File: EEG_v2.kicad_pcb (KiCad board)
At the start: 2 copper layers, 114 parts, among them P1 CONN_2, P2 CONN_8, P3 USB_A, P4 CONN_8, P5 CONN_5X2, P6 CONN_2, P7 CONN_1, SW1 SWITCH_INV, SW2 RESET, SW3 SW_PUSH_4PIN, SW4 SW_PUSH_4PIN, U1 ADS1299IPAGR, U2 TLV70033, U3 TLV70025, U4 LM2664, U5 TPS72325, U6 CC2540, U7 2450BM15A0002E, X1 QUARTZCMS4_32K, X2 32-MHz

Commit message: Continue layout.
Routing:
- net N-0000096: track 0.00 -> 1.18 mm
- net N-0000094: track 0.00 -> 1.18 mm
- net N-0000093: track 0.00 -> 1.18 mm
- net N-0000092: track 0.00 -> 1.18 mm
- net N-0000091: track 0.00 -> 1.18 mm
- net N-0000090: track 0.00 -> 1.18 mm
- net N-0000089: track 0.00 -> 1.18 mm
- net N-0000088: track 0.00 -> 1.18 mm
- net N-0000078: track 0.00 -> 1.18 mm
- net N-0000077: track 0.00 -> 1.18 mm
- net N-0000076: track 0.00 -> 1.18 mm
- net N-0000070: track 0.00 -> 1.18 mm
- net N-0000067: track 0.00 -> 1.18 mm
- net N-0000095: track 0.00 -> 1.18 mm
- net N-0000079: track 0.00 -> 1.18 mm
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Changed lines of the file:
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@@
   (general
     (links 295)
-    (no_connects 193)
+    (no_connects 177)
     (area 249.516999 132.753099 336.86877 191.129001)
     (thickness 1.6)
-    (drawings 0)
-    (tracks 263)
+    (drawings 1)
+    (tracks 295)
     (zones 0)
     (modules 114)
@@
     )
   )
+  (dimension 43.501839 (width 0.3) (layer F.SilkS)
+    (gr_text "43.502 mm" (at 345.328961 154.844059 89.47315711) (layer F.SilkS)
+      (effects (font (size 1.5 1.5) (thickness 0.3)))
+    )
+    (feature1 (pts (xy 334.9 176.5) (xy 346.478904 176.606472)))
+    (feature2 (pts (xy 335.3 133) (xy 346.878904 133.106472)))
+    (crossbar (pts (xy 344.179019 133.081646) (xy 343.779019 176.581646)))
+    (arrow1a (pts (xy 343.779019 176.581646) (xy 343.202982 175.449798)))
+    (arrow1b (pts (xy 343.779019 176.581646) (xy 344.375773 175.460583)))
+    (arrow2a (pts (xy 344.179019 133.081646) (xy 343.582265 134.202709)))
+    (arrow2b (pts (xy 344.179019 133.081646) (xy 344.755056 134.213494)))
+  )
   (segment (start 311.85184 165.74816) (end 311.85184 165.35184) (width 0.254) (layer F.Cu) (net 1))
   (segment (start 310.93156 164.43156) (end 310.93156 162.90544) (width 0.254) (layer F.Cu) (net 1))
@@
   (segment (start 305.27116 172.67884) (end 305.27116 170.58) (width 0.254) (layer F.Cu) (net 59))
   (segment (start 304.957 172.993) (end 305.27116 172.67884) (width 0.254) (layer F.Cu) (net 59))
+  (segment (start 327.1005 142.9385) (end 327.1005 143.9815) (width 0.254) (layer F.Cu) (net 66) (status C00000))
+  (segment (start 327.1005 143.9815) (end 327.2005 144.0815) (width 0.254) (layer F.Cu) (net 66) (status C00000))
+  (segment (start 327.1005 137.3505) (end 327.1005 136.3075) (width 0.254) (layer F.Cu) (net 67) (status C00000))
+  (segment (start 327.1005 136.3075) (end 327.2005 136.2075) (width 0.254) (layer F.Cu) (net 67) (status C00000))
+  (segment (start 327.1005 138.4935) (end 327.1005 139.5365) (width 0.254) (layer F.Cu) (net 68) (status C00000))
+  (segment (start 327.1005 139.5365) (end 327.2005 139.6365) (width 0.254) (layer F.Cu) (net 68) (status C00000))
+  (segment (start 327.1005 147.3835) (end 327.1005 148.4265) (width 0.254) (layer F.Cu) (net 69) (status C00000))
+  (segment (start 327.1005 148.4265) (end 327.2005 148.5265) (width 0.254) (layer F.Cu) (net 69) (status C00000))
+  (segment (start 327.1005 141.7955) (end 327.1005 140.7525) (width 0.254) (layer F.Cu) (net 70) (status C00000))
+  (segment (start 327.1005 140.7525) (end 327.2005 140.6525) (width 0.254) (layer F.Cu) (net 70) (status C00000))
+  (segment (start 327.1005 146.2405) (end 327.1005 145.1975) (width 0.254) (layer F.Cu) (net 71) (status C00000))
+  (segment (start 327.1005 145.1975) (end 327.2005 145.0975) (width 0.254) (layer F.Cu) (net 71) (status C00000))
+  (segment (start 327.1005 150.6855) (end 327.1005 149.6425) (width 0.254) (layer F.Cu) (net 72) (status C00000))
+  (segment (start 327.1005 149.6425) (end 327.2005 149.5425) (width 0.254) (layer F.Cu) (net 72) (status C00000))
+  (segment (start 327.1005 169.7355) (end 327.1005 170.7785) (width 0.254) (layer F.Cu) (net 74) (status C00000))
+  (segment (start 327.1005 170.7785) (end 327.2005 170.8785) (width 0.254) (layer F.Cu) (net 74) (status C00000))
+  (segment (start 327.1005 168.5925) (end 327.1005 167.5495) (width 0.254) (layer F.Cu) (net 75) (status C00000))
+  (segment (start 327.1005 167.5495) (end 327.2005 167.4495) (width 0.254) (layer F.Cu) (net 75) (status C00000))
+  (segment (start 327.1005 159.5755) (end 327.1005 158.5325) (width 0.254) (layer F.Cu) (net 76) (status C00000))
+  (segment (start 327.1005 158.5325) (end 327.2005 158.4325) (width 0.254) (layer F.Cu) (net 76) (status C00000))
+  (segment (start 327.1005 160.7185) (end 327.1005 161.7615) (width 0.254) (layer F.Cu) (net 77) (status C00000))
+  (segment (start 327.1005 161.7615) (end 327.2005 161.8615) (width 0.254) (layer F.Cu) (net 77) (status C00000))
+  (segment (start 327.1005 164.0205) (end 327.1005 162.9775) (width 0.254) (layer F.Cu) (net 78) (status C00000))
+  (segment (start 327.1005 162.9775) (end 327.2005 162.8775) (width 0.254) (layer F.Cu) (net 78) (status C00000))
+  (segment (start 327.1005 165.1635) (end 327.1005 166.2065) (width 0.254) (layer F.Cu) (net 79) (status C00000))
+  (segment (start 327.1005 166.2065) (end 327.2005 166.3065) (width 0.254) (layer F.Cu) (net 79) (status C00000))
+  (segment (start 327.1005 151.8285) (end 327.1005 152.8715) (width 0.254) (layer F.Cu) (net 80) (status C00000))
+  (segment (start 327.1005 152.8715) (end 327.2005 152.9715) (width 0.254) (layer F.Cu) (net 80) (status C00000))
+  (segment (start 327.1005 156.2735) (end 327.1005 157.3165) (width 0.254) (layer F.Cu) (net 81) (status C00000))
+  (segment (start 327.1005 157.3165) (end 327.2005 157.4165) (width 0.254) (layer F.Cu) (net 81) (status C00000))
+  (segment (start 327.1005 155.1305) (end 327.1005 154.0875) (width 0.254) (layer F.Cu) (net 82) (status C00000))
+  (segment (start 327.1005 154.0875) (end 327.2005 153.9875) (width 0.254) (layer F.Cu) (net 82) (status C00000))
   (segment (start 292.9415 144.5455) (end 291.252 144.5455) (width 0.254) (layer F.Cu) (net 83))
   (segment (start 291.252 144.5455) (end 290.75 145.0475) (width 0.254) (layer F.Cu) (net 83))

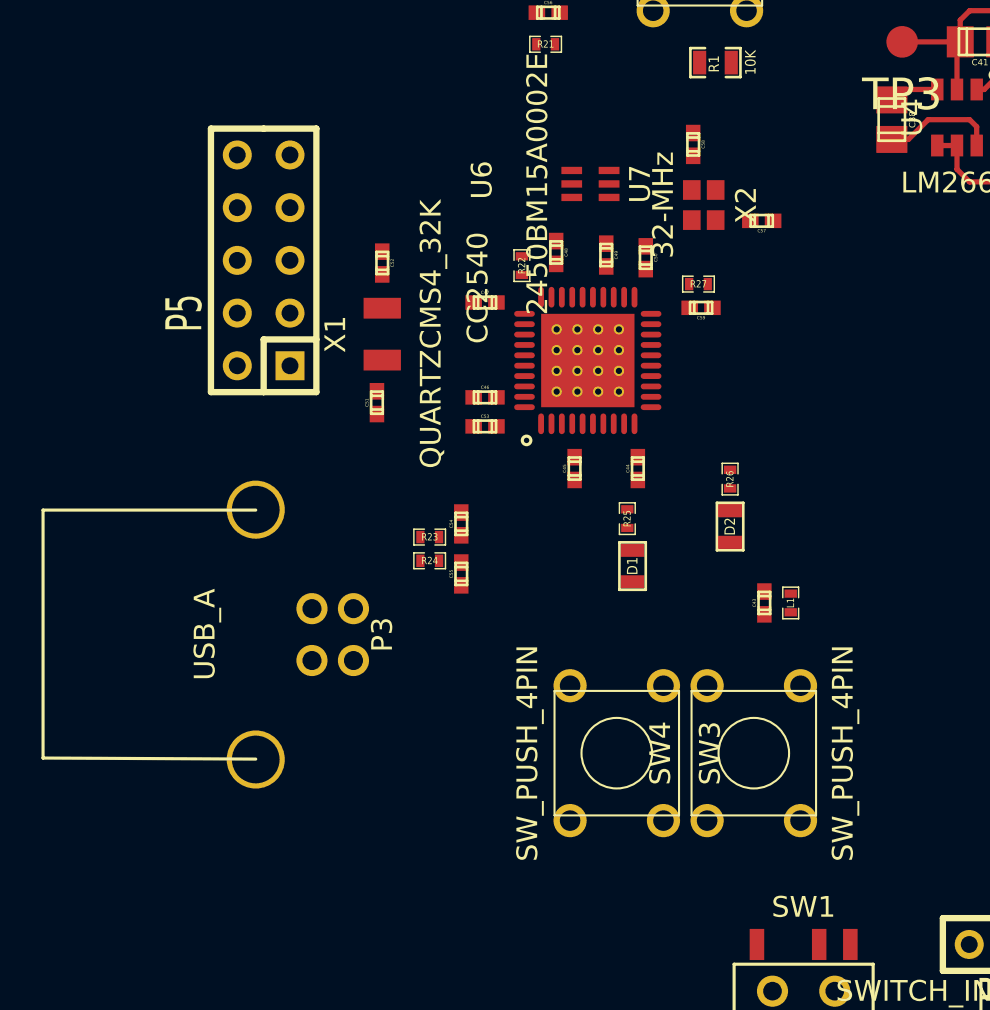
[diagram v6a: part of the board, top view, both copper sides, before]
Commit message: Continue layout for CC2540
Change swiches to one pin operating to clear under space. Edit USB conn
to show back size.
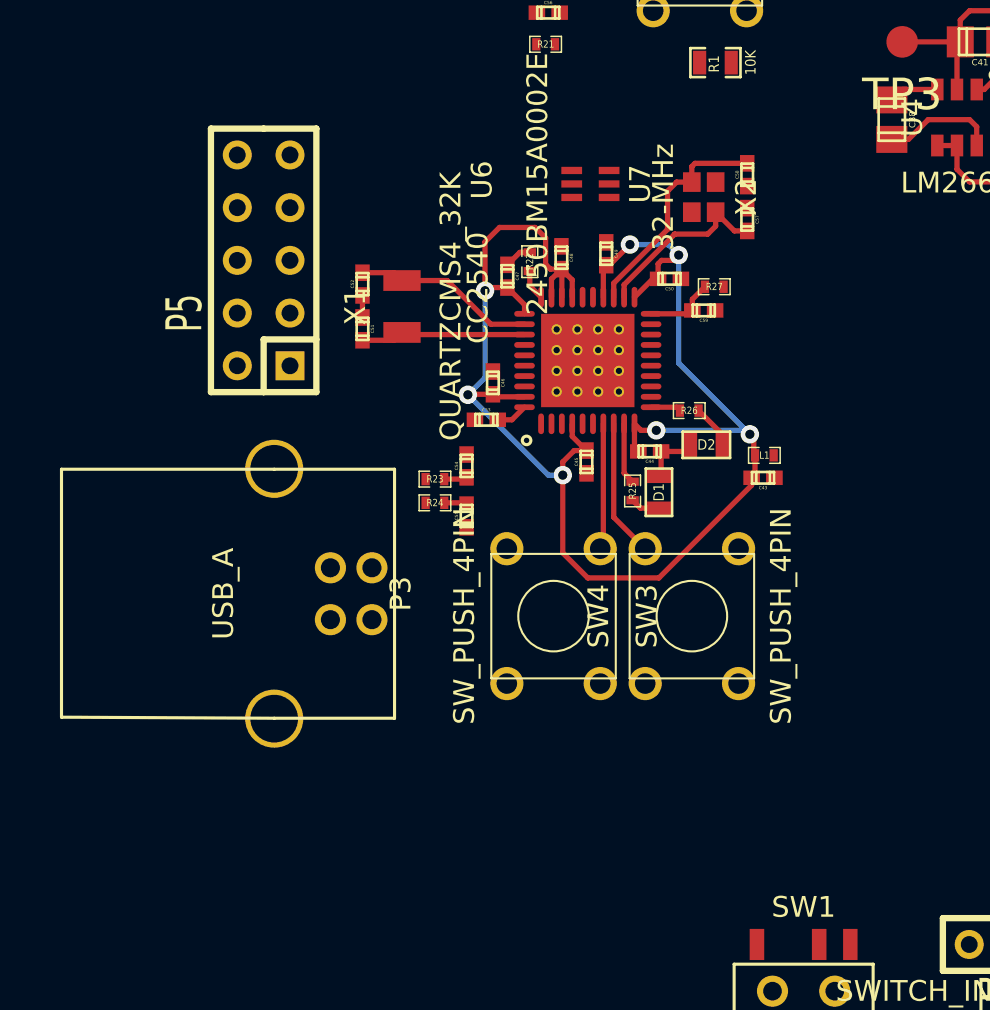
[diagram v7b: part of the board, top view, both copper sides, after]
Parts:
- moved SW3 7.27 mm to (274.4, 169.9)
- moved SW4 7.25 mm to (281.1, 169.9)
- moved L1 7.22 mm to (284.6, 162.2), turned to 0 degrees
- moved C43 6.03 mm to (284.5, 163.3), turned to 180 degrees
- moved D2 4.10 mm to (281.8, 161.7), turned to 180 degrees
- moved R26 3.84 mm to (281.0, 160.0), turned to 180 degrees
- moved D1 3.78 mm to (279.5, 164.0), turned to 90 degrees
- moved C51 3.62 mm to (265.2, 156.1), turned to 270 degrees
- moved C58 2.99 mm to (283.8, 148.7), turned to 90 degrees
- moved R23 2.81 mm to (268.7, 163.3), turned to 0 degrees
- moved C55 2.81 mm to (270.3, 165.1)
- moved R24 2.81 mm to (268.7, 164.5)
- moved C54 2.81 mm to (270.3, 162.7)
- moved P3 2.16 mm to (261.0, 168.8)
- moved C47 1.67 mm to (272.2, 153.5), turned to 270 degrees
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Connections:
- SW3 pad 3: /Microcontroller/SW3 -> (no net)
- SW4 pad 4: /Microcontroller/SW4 -> (no net)
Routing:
- net /Microcontroller/VDD_FILT: track 0.00 -> 77.0 mm, vias 0 -> 7
- net /Microcontroller/X2_3: track 0.00 -> 11.1 mm
- net /Microcontroller/X1_2: track 0.00 -> 8.84 mm
- net /Microcontroller/X2_1: track 0.00 -> 8.80 mm
- net /Microcontroller/X1_1: track 0.00 -> 8.01 mm
- net /Microcontroller/SW4: track 0.00 -> 6.65 mm
- net /Microcontroller/SW3: track 0.00 -> 6.08 mm
- net AGND: track 134.9 -> 140.1 mm
- net /Microcontroller/RESET_INTR: track 0.00 -> 3.45 mm
- net /Microcontroller/LED1: track 0.00 -> 2.96 mm
- net N-0000053: track 0.00 -> 2.12 mm
- net N-0000049: track 0.00 -> 1.54 mm
- net N-0000043: track 0.00 -> 1.49 mm
- net /Microcontroller/LED2: track 0.00 -> 1.46 mm
- net N-0000052: track 0.00 -> 1.43 mm
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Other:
- net class Comp: clearance 0.127 -> 0.1524
- net class RF_Diff added: clearance 0.127, trace_width 0.254, via_dia 0.889, via_drill 0.635

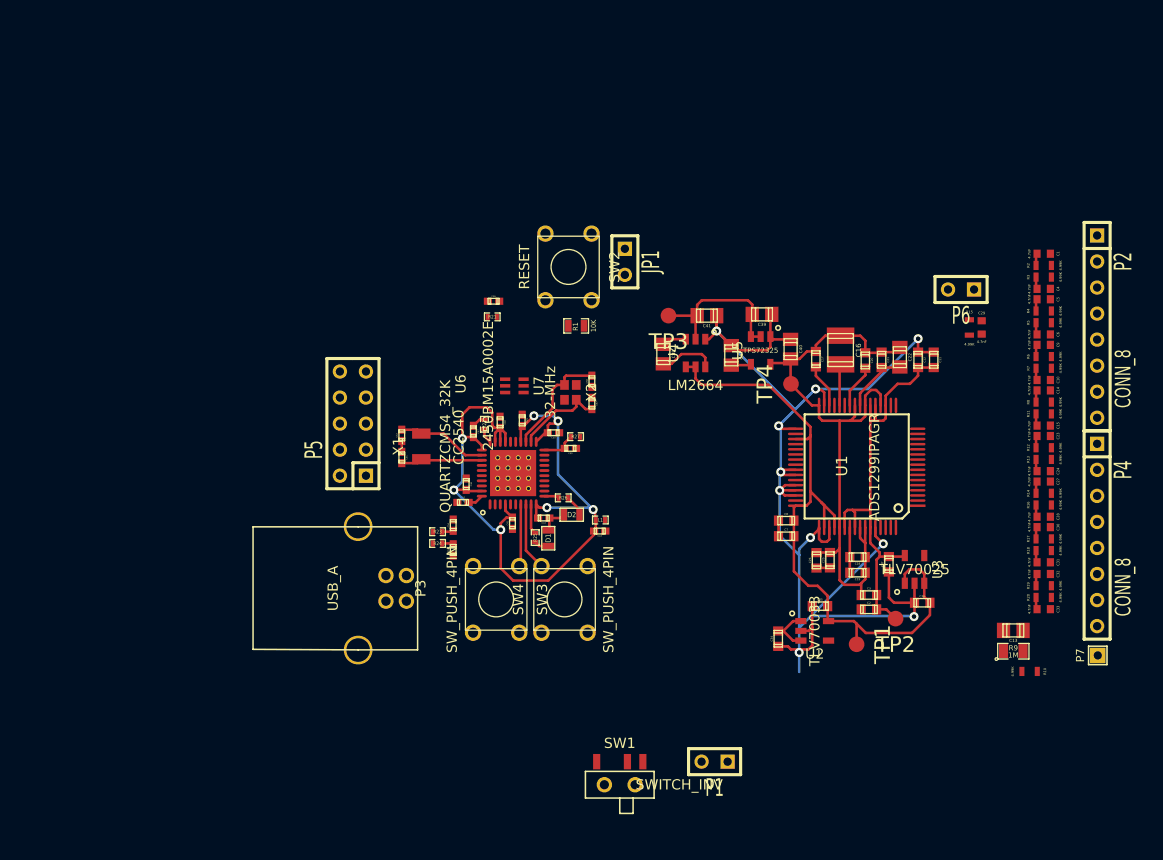
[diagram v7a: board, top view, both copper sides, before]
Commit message: Continue layout, compress chips together.
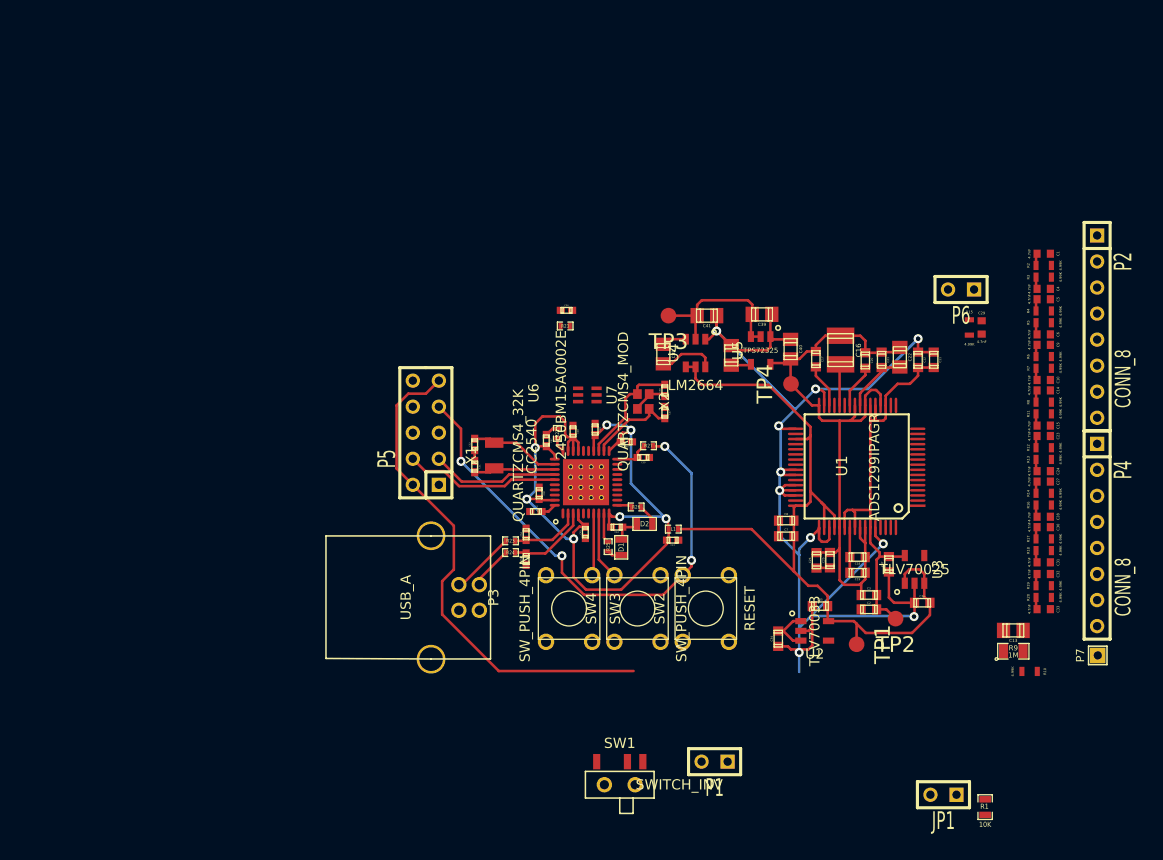
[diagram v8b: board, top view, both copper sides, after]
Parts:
- X2: value 32-MHz -> QUARTZCMS4_MOD
- moved R1 61.6 mm to (322.1, 190.2), turned to 90 degrees
- moved JP1 60.6 mm to (318.1, 189.0), turned to 180 degrees
- moved SW2 35.9 mm to (294.9, 170.8), turned to 90 degrees
- moved C43 7.17 mm to (291.7, 164.1)
- moved C44 7.17 mm to (286.2, 162.9)
- moved C45 7.17 mm to (283.1, 163.4)
- moved C48 7.17 mm to (281.9, 153.5)
- moved C55 7.17 mm to (277.4, 166.0)
- moved C56 7.17 mm to (281.3, 141.7)
- moved C57 7.17 mm to (290.9, 151.7)
- moved C59 7.17 mm to (288.8, 156.1)
- moved D1 7.17 mm to (286.6, 164.8)
- moved D2 7.17 mm to (288.9, 162.6)
- moved R21 7.17 mm to (281.2, 143.3)
- moved R25 7.17 mm to (285.4, 164.8)
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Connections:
- SW2 pad 4: /Microcontroller/RESET_N -> (no net)
- X2 pad 2: (no net) -> AGND
- X2 pad 4: (no net) -> AGND
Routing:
- net /Microcontroller/RESET_N: track 0.00 -> 50.2 mm, vias 0 -> 4
- net VIN_RAW: track 5.20 -> 54.5 mm
- net /Microcontroller/DD: track 0.00 -> 15.2 mm
- net +3.3V: track 66.5 -> 79.6 mm
- net /Microcontroller/DC: track 0.00 -> 12.5 mm
- net /Microcontroller/USB_N_Intr: track 1.11 -> 8.01 mm
- net /Microcontroller/USB_P: track 0.00 -> 6.36 mm
- net /Microcontroller/USB_P_Intr: track 1.11 -> 6.89 mm
- net /Microcontroller/USB_N: track 0.00 -> 4.20 mm
- net AGND: track 140.1 -> 143.6 mm
